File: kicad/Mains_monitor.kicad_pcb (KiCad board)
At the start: 2 copper layers, 69 x 89 mm, 34 parts, among them J1 Screw_Terminal_01x02, J2 Screw_Terminal_01x02, K1 SANYOU_SRD_Form_C, Q1 Q_NPN_CBE, U1 HLW8032

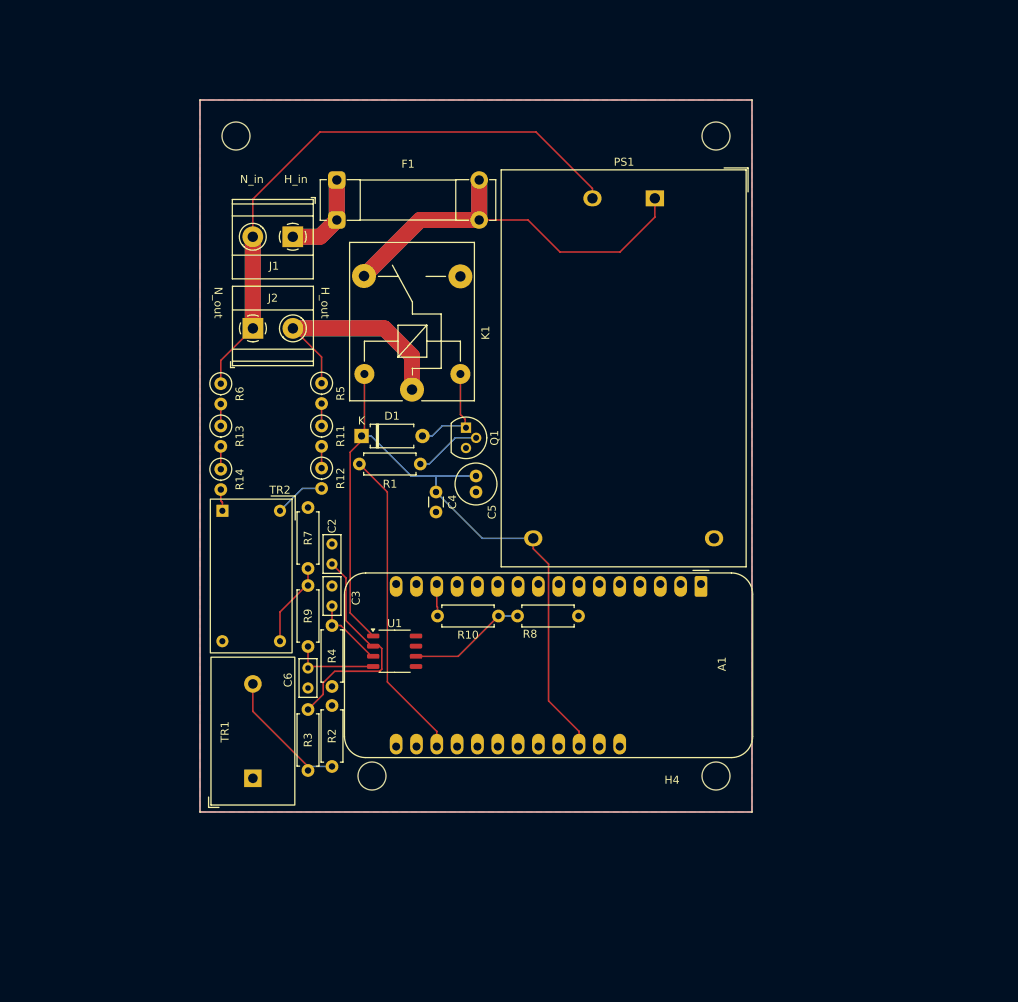
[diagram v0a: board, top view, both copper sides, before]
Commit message: added power supply fuse, increased high current trace size, Ready to order
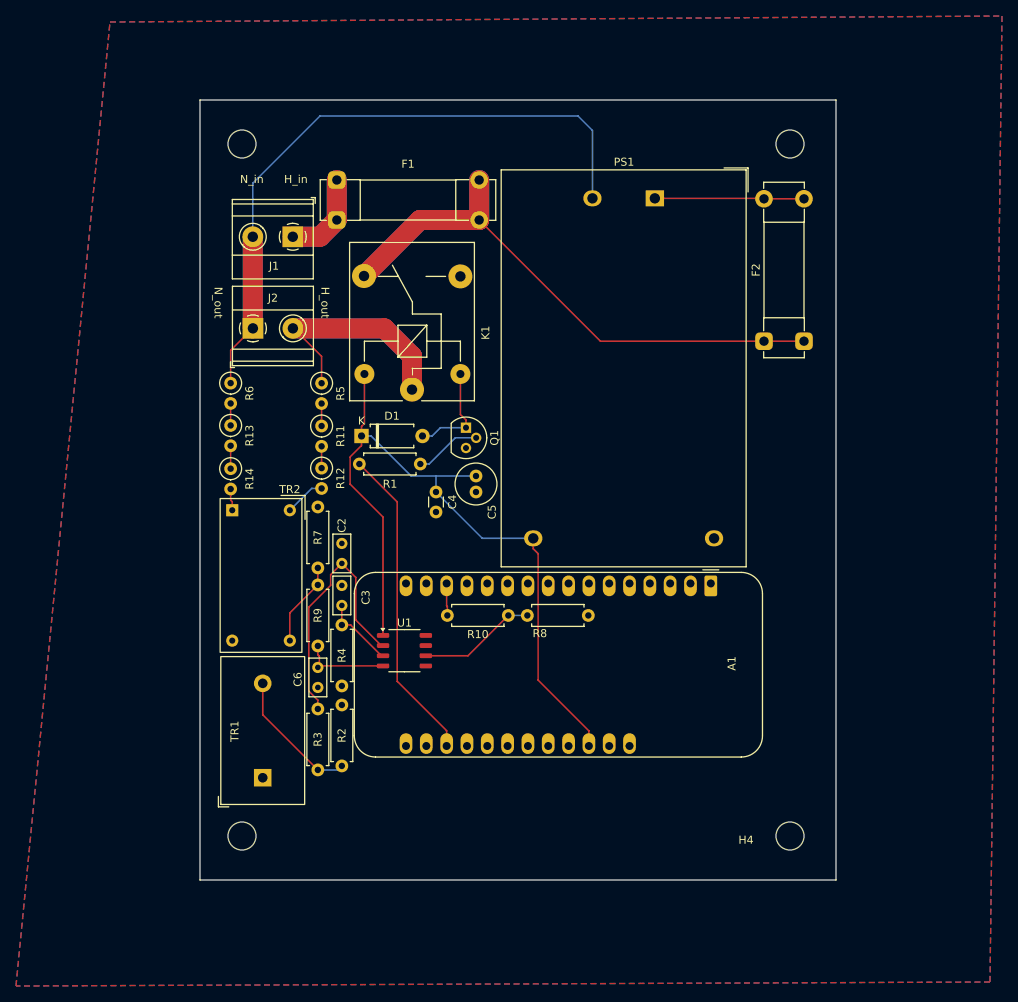
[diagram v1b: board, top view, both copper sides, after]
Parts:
- added F2: 100mAx250V, Fuse:Fuseholder_Clip-5x20mm_Bel_FC-203-22_Lateral_P17.80x5.00mm_D1.17mm_Horizontal, F.Cu at (161.0, 75.2)
- moved H3 17.9 mm to (95.8, 137.0)
- moved H4 11.9 mm to (164.2, 137.0)
- moved H2 9.30 mm to (164.2, 50.5)
- moved H1 1.25 mm to (95.8, 50.5)
- moved R14 1.23 mm to (94.3, 91.1)
- moved R4 1.23 mm to (108.2, 118.2)
- moved U1 1.23 mm to (116.1, 113.8)
- moved C2 1.23 mm to (108.2, 102.9)
- moved C3 1.23 mm to (108.2, 105.7)
- moved C6 1.23 mm to (105.2, 115.9)
- moved R13 1.23 mm to (94.3, 85.7)
- moved R2 1.23 mm to (108.2, 128.2)
- moved R3 1.23 mm to (105.2, 128.7)
- moved R6 1.23 mm to (94.3, 80.4)
- moved R7 1.23 mm to (105.2, 95.9)
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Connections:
- PS1 pad 1: AC_H -> Net-(PS1-AC/L)
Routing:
- net AC_H: track 72.4 -> 91.5 mm
- net Net-(PS1-AC/L): track 0.00 -> 18.6 mm
- net AC_N: track 87.0 -> 93.7 mm
- net IP: track 28.5 -> 32.9 mm
- net Net-(R12-Pad2): track 6.36 -> 5.10 mm
- net Net-(R2-Pad1): track 16.2 -> 16.9 mm
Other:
- board size 69 x 89 mm -> 79.5 x 97.5 mm

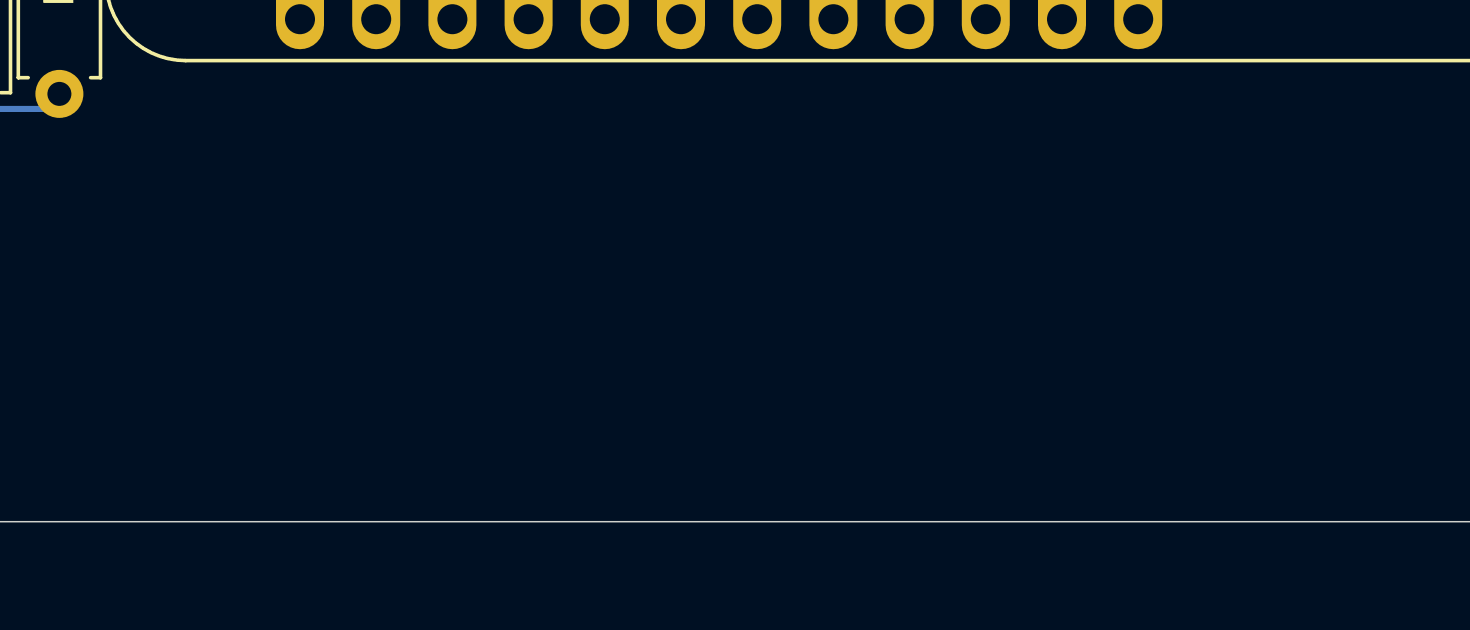
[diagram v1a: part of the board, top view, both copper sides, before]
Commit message: Added 'Energy Meeter Rev A' to silkscreen
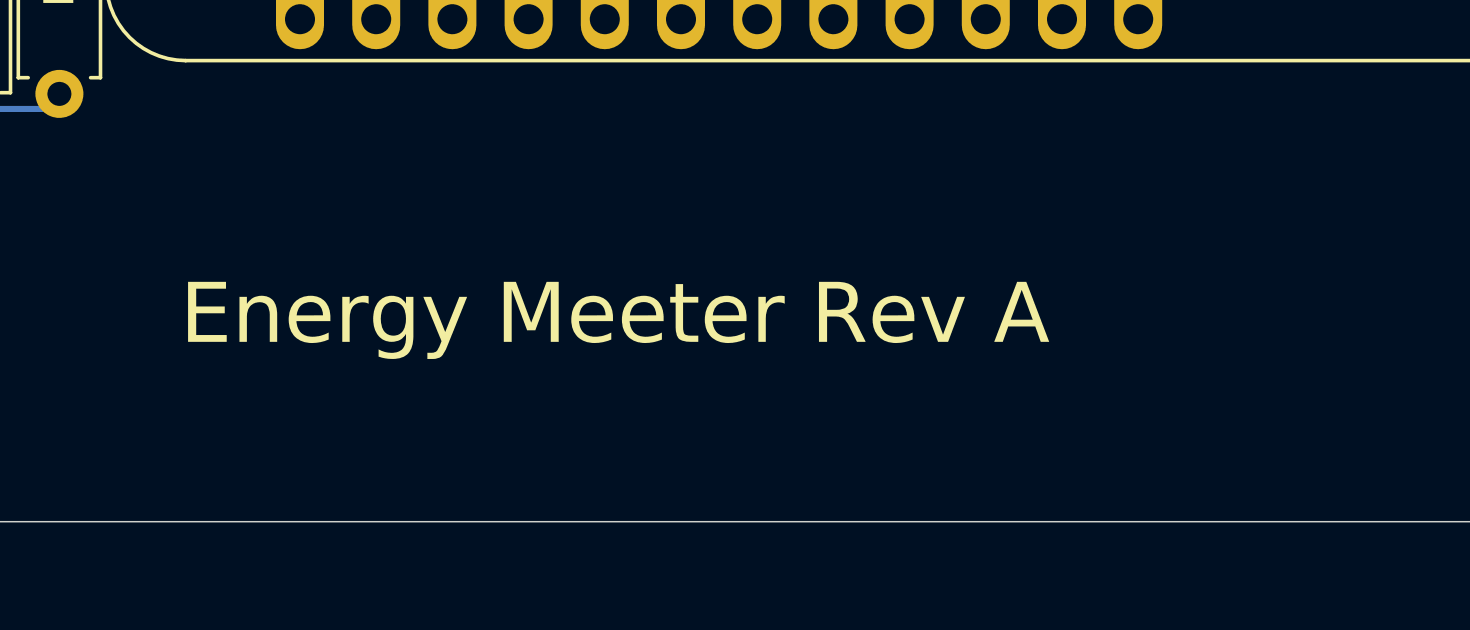
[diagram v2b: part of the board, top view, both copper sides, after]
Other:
- board text added: "Energy Meeter Rev A"
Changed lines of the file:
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@@
+		)
+	)
+	(gr_text "Energy Meeter Rev A"
+		(at 112.25 136.75 0)
+		(layer "F.SilkS")
+		(effects
+			(font
+				(size 2 2)
+				(thickness 0.1)
+			)
+			(justify left bottom)
 		)
 	)
